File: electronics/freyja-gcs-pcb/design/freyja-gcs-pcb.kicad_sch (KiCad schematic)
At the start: 26 parts, among them J1 Conn_01x07_Pin, SW1 SW_SPST, SW2 SW_SPST, U1 STM32U575RGTx, U2 GT-USB-7010ASV, Y1 48MHz, Y2 32768Hz

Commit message: tvs diodes
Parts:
- added C13: 100p, symbol Device:C_Small
- added D2, D3, D4, D5: 0603ESDA-05N, Diode_SMD:D_0603_1608Metric_Pad1.05x0.95mm_HandSolder, symbol Device:D_TVS
- C3: value 10n -> 100p
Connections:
- net BOOT0: now also C13.1, D5.1 (A1)
- net GND: now also C13.2, D2.2 (A2), D3.2 (A2), D4.2 (A2), D5.2 (A2)
- net NRST: now also D4.1 (A1)
- net USB_D_N: now also D2.1 (A1)
- net USB_D_P: now also D3.1 (A1)
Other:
- moved on the sheet: C3, R2, SW2

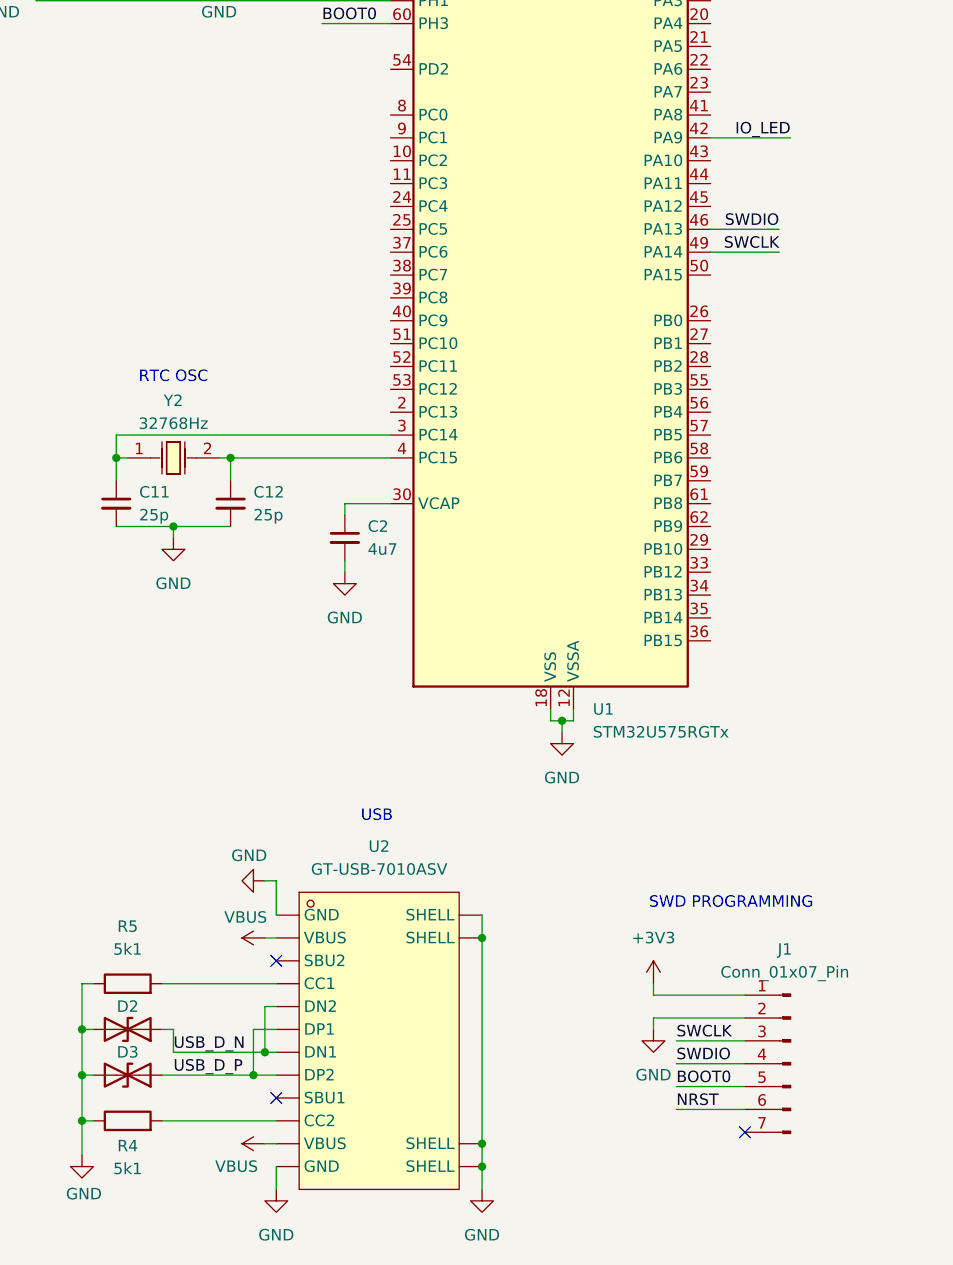
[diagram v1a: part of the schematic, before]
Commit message: add usb diff directive
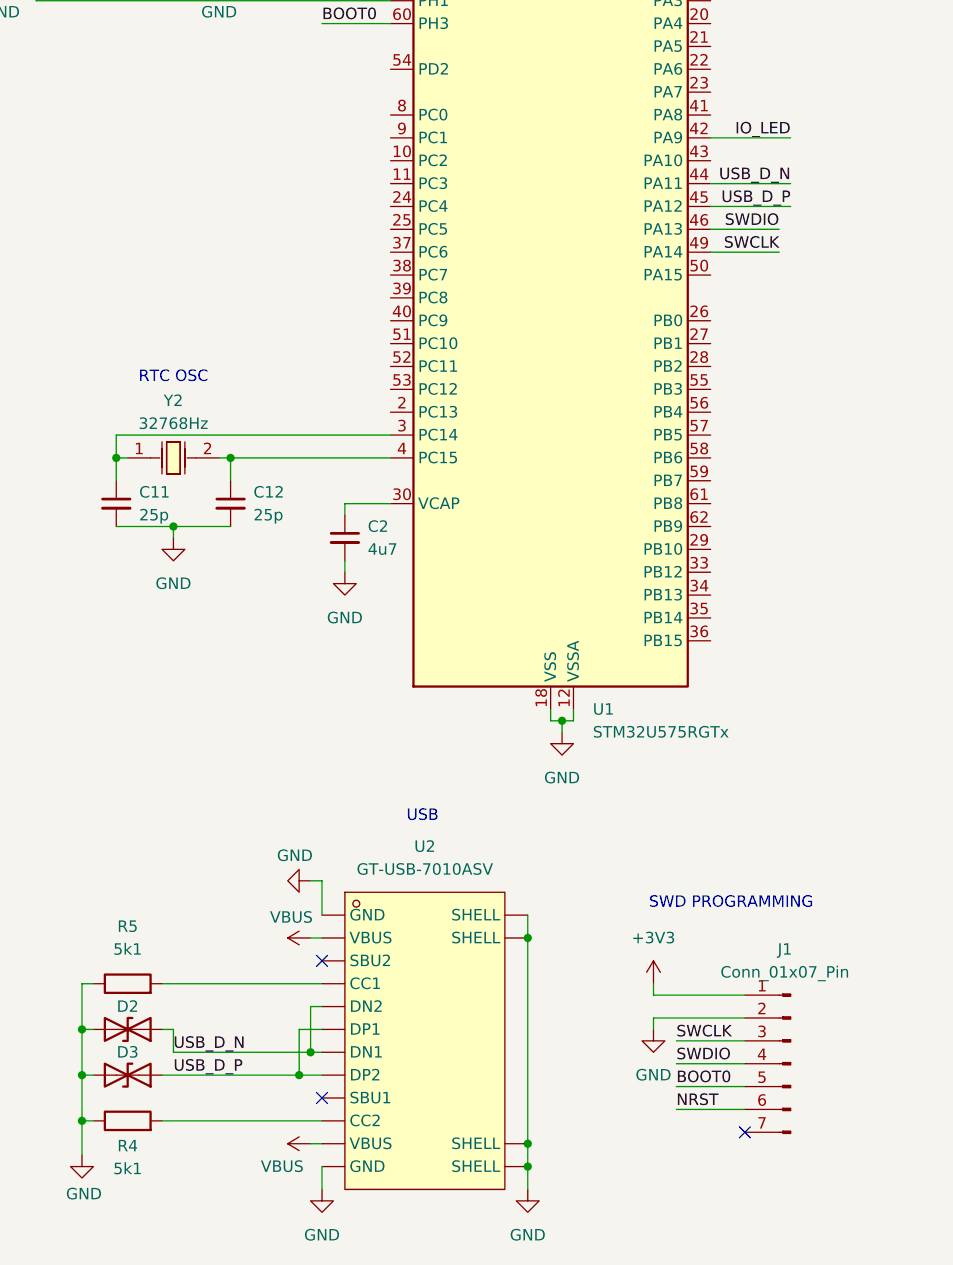
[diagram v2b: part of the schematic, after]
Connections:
- net USB_D_N: now also U1.44 (PA11)
- net USB_D_P: now also U1.45 (PA12)
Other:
- moved on the sheet: U2

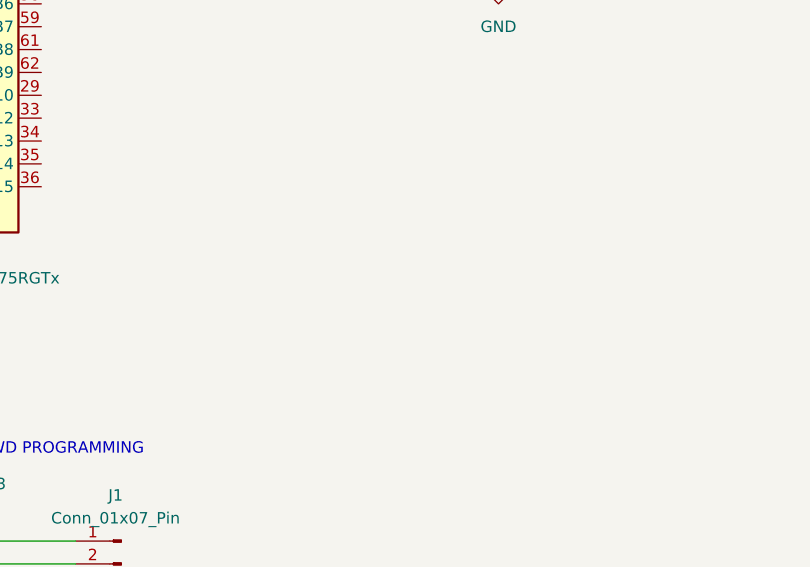
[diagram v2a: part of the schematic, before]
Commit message: Added switches and LEDs for the GCB.
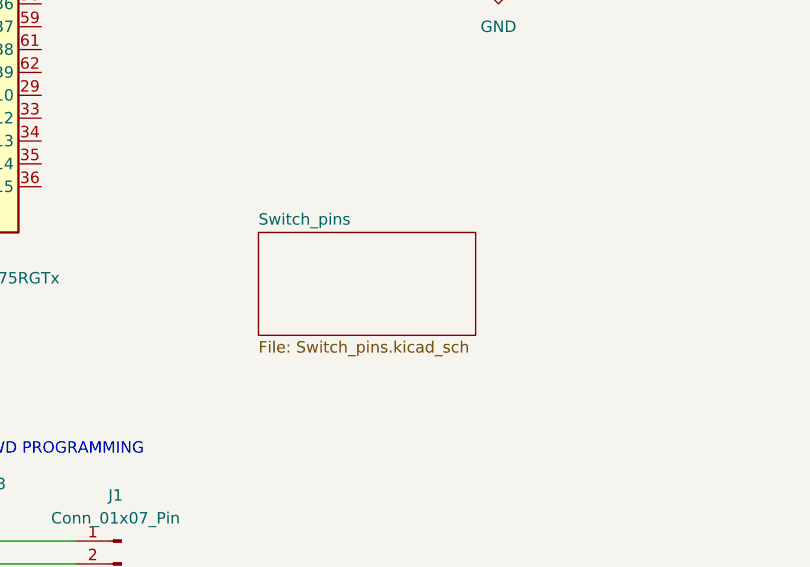
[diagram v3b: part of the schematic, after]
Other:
- added sheet Switch_pins (Switch_pins.kicad_sch)
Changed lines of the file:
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@@
+		)
+	)
+	(sheet
+		(at 120.65 124.46)
+		(size 24.13 11.43)
+		(exclude_from_sim no)
+		(in_bom yes)
+		(on_board yes)
+		(dnp no)
+		(fields_autoplaced yes)
+		(stroke
+			(width 0.1524)
+			(type solid)
+		)
+		(fill
+			(color 0 0 0 0.0000)
+		)
+		(property "Sheetname" "Switch_pins"
+			(at 120.65 123.7484 0)
+			(effects
+				(font
+					(size 1.27 1.27)
+				)
+				(justify left bottom)
+			)
+		)
+		(property "Sheetfile" "Switch_pins.kicad_sch"
+			(at 120.65 136.4746 0)
+			(effects
+				(font
+					(size 1.27 1.27)
+				)
+				(justify left top)
+			)
+		)
+		(instances
+			(project "freyja-gcs-pcb"
+				(path "/c292fa04-82ad-49e9-a9d8-422554d1d11d"
+					(page "2")
+				)
+			)
 		)
 	)

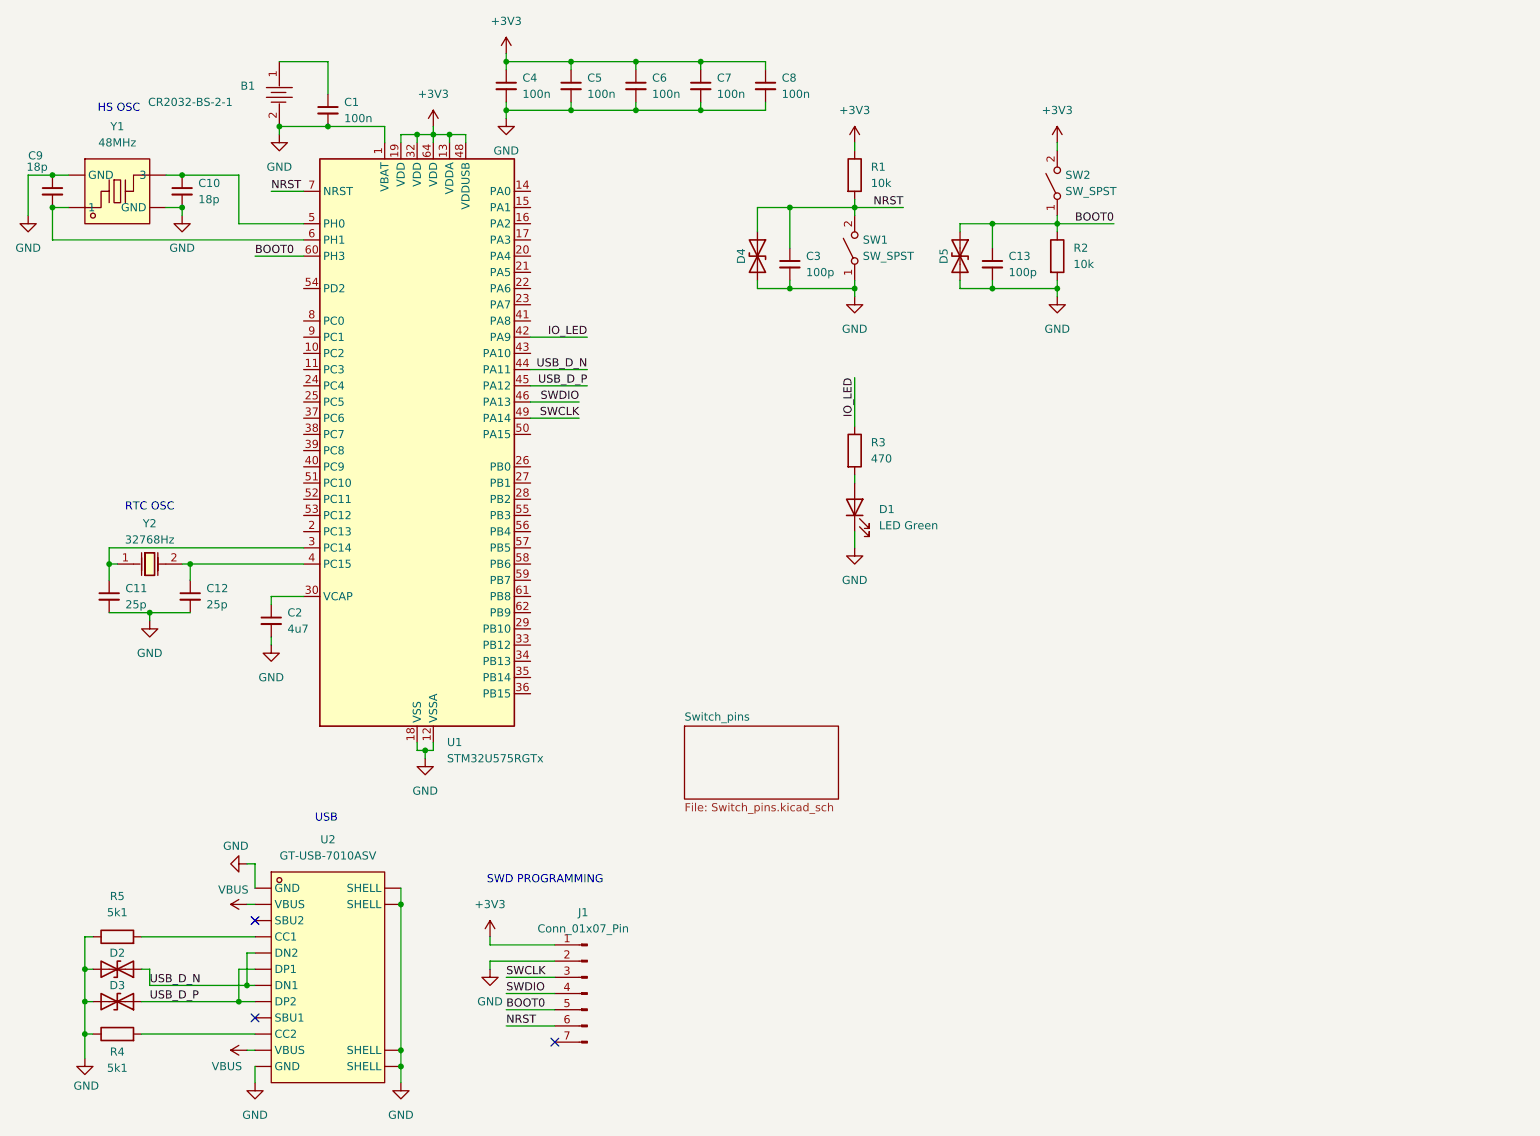
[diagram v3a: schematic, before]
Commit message: Added FDCAN interface. Connector has to be added!!
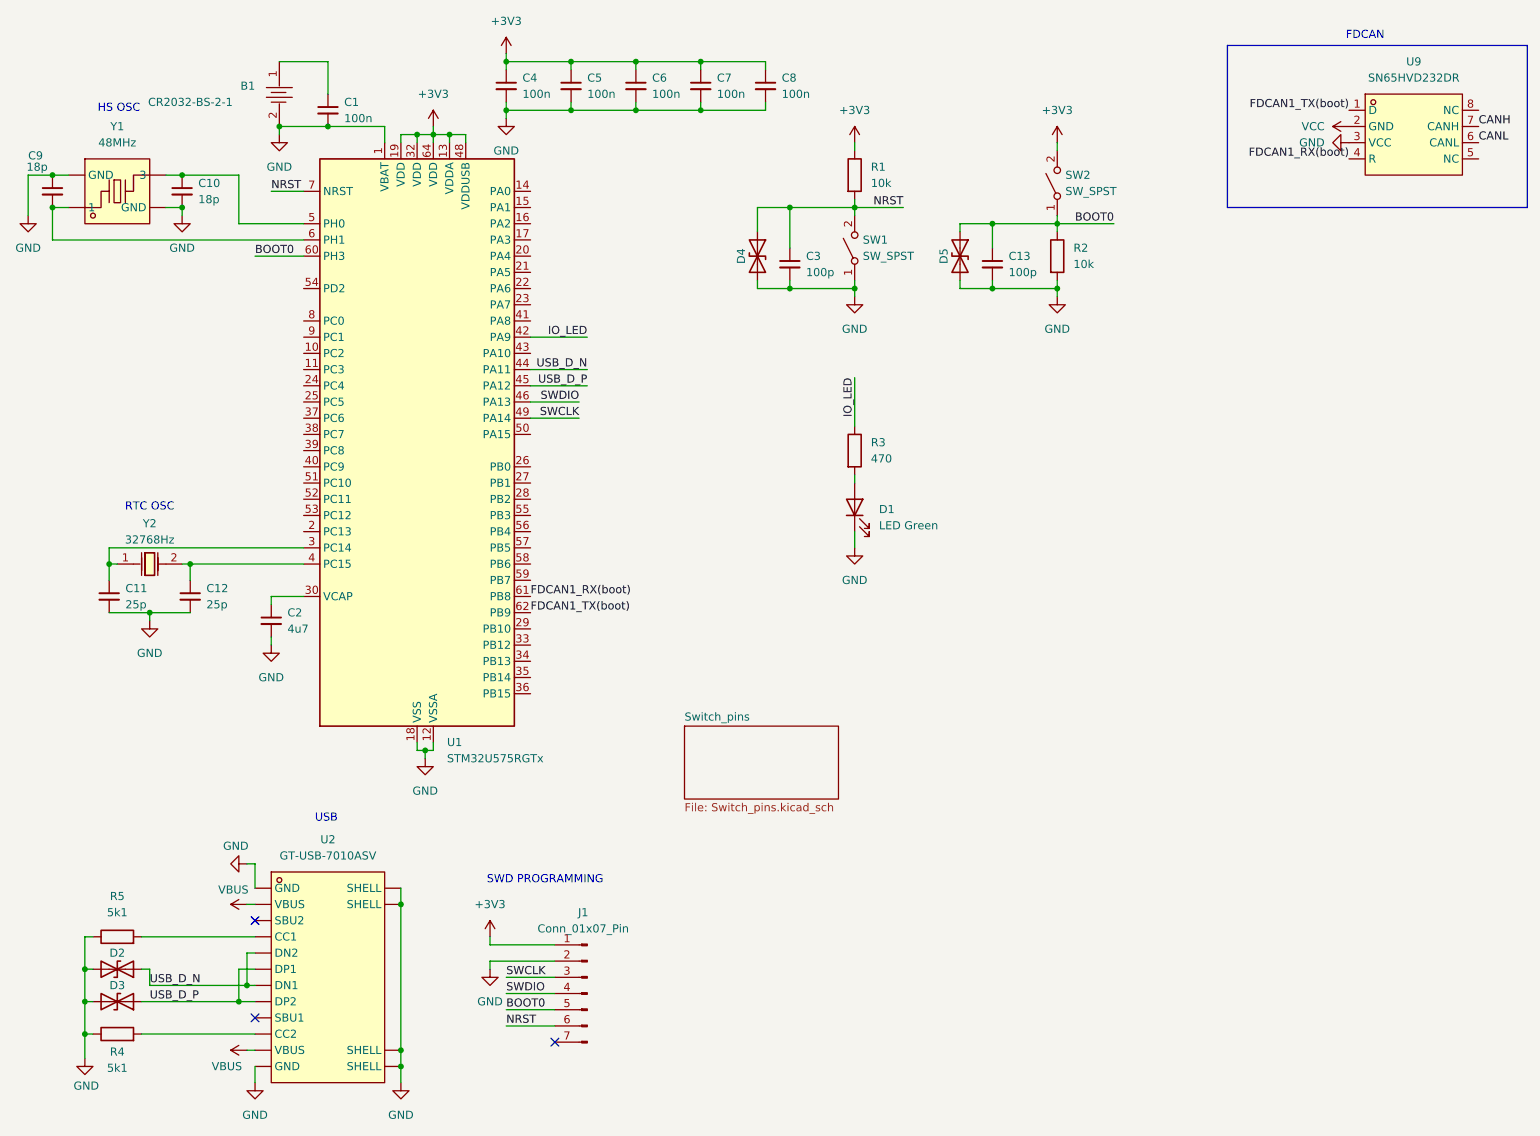
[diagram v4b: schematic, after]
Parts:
- added U9: SN65HVD232DR, EasyEDA:SOIC-8_L5.0-W4.0-P1.27-LS6.0-BL, symbol EasyEDA:SN65HVD232DR
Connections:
- net GND: now also U9.3 (VCC)
- net FDCAN1_RX(boot): now reaches U1.61 (PB8)
- net FDCAN1_RX(boot): now also U9.4 (R)
- net FDCAN1_TX(boot): now reaches U1.62 (PB9)
- net FDCAN1_TX(boot): now also U9.1 (D)
- new net CANH: U9.7 (CANH)
- new net CANL: U9.6 (CANL)
- new net VCC: U9.2 (GND)
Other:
- note added: "FDCAN"

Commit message: add power circuit
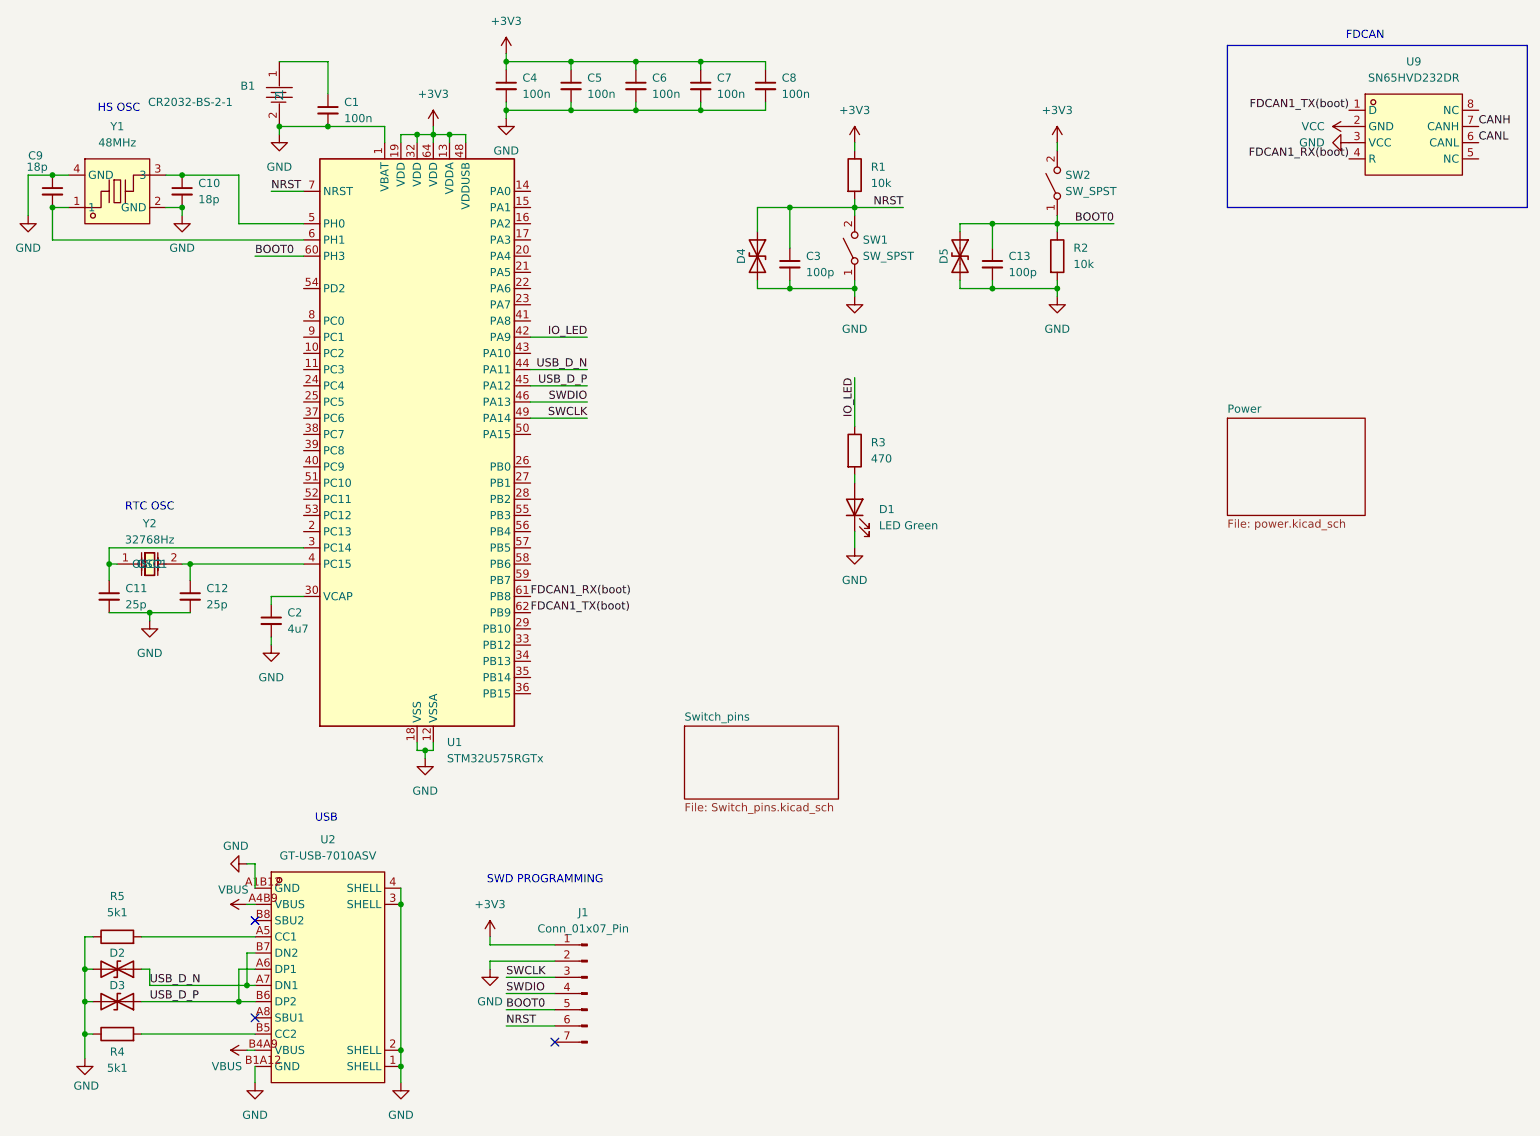
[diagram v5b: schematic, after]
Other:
- added sheet Power (power.kicad_sch)
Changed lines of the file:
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@@
 	(wire
 		(pts
-			(xy 96.52 73.66) (xy 104.14 73.66)
+			(xy 96.52 73.66) (xy 105.41 73.66)
 		)
 		(stroke
@@
 	(wire
 		(pts
-			(xy 96.52 76.2) (xy 104.14 76.2)
+			(xy 96.52 76.2) (xy 105.41 76.2)
 		)
 		(stroke
@@
 	)
 	(label "SWCLK"
-		(at 104.14 76.2 180)
+		(at 105.41 76.2 180)
 		(effects
 			(font
@@
 	)
 	(label "SWDIO"
-		(at 104.14 73.66 180)
+		(at 105.41 73.66 180)
 		(effects
 			(font
@@
 			(effects
 				(font
+					(size 1.27 1.27)
+				)
+				(justify left top)
+			)
+		)
+		(instances
+			(project "freyja-gcs-pcb"
+				(path "/c292fa04-82ad-49e9-a9d8-422554d1d11d"
+					(page "2")
+				)
+			)
+		)
+	)
+	(sheet
+		(at 205.74 76.2)
+		(size 21.59 15.24)
+		(exclude_from_sim no)
+		(in_bom yes)
+		(on_board yes)
+		(dnp no)
+		(fields_autoplaced yes)
+		(stroke
+			(width 0.1524)
+			(type solid)
+		)
+		(fill
+			(color 0 0 0 0.0000)
+		)
+		(property "Sheetname" "Power"
+			(at 205.74 75.4884 0)
+			(effects
+				(font
+					(size 1.27 1.27)
+				)
+				(justify left bottom)
+			)
+		)
+		(property "Sheetfile" "power.kicad_sch"
+			(at 205.74 92.0246 0)
+			(effects
+				(font
